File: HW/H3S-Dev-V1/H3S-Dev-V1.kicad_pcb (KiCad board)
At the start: 2 copper layers, 85 x 56 mm, 70 parts, among them J1 USB_C_Receptacle_USB2.0_16P, J2 Conn_01x02, J3 Conn_Coaxial, J4 Conn_01x04, J5 Conn_01x04, Q1 DMP3099L, SW1 SW_Push, SW2 SW_Push, U1 Ra-01SH-P, U2 LTC4054ES5-4.2, U3 USBLC6-2SC6, U4 ESP32-S3-WROOM-1, U5 SY8089AAAC, U6 L96-M33

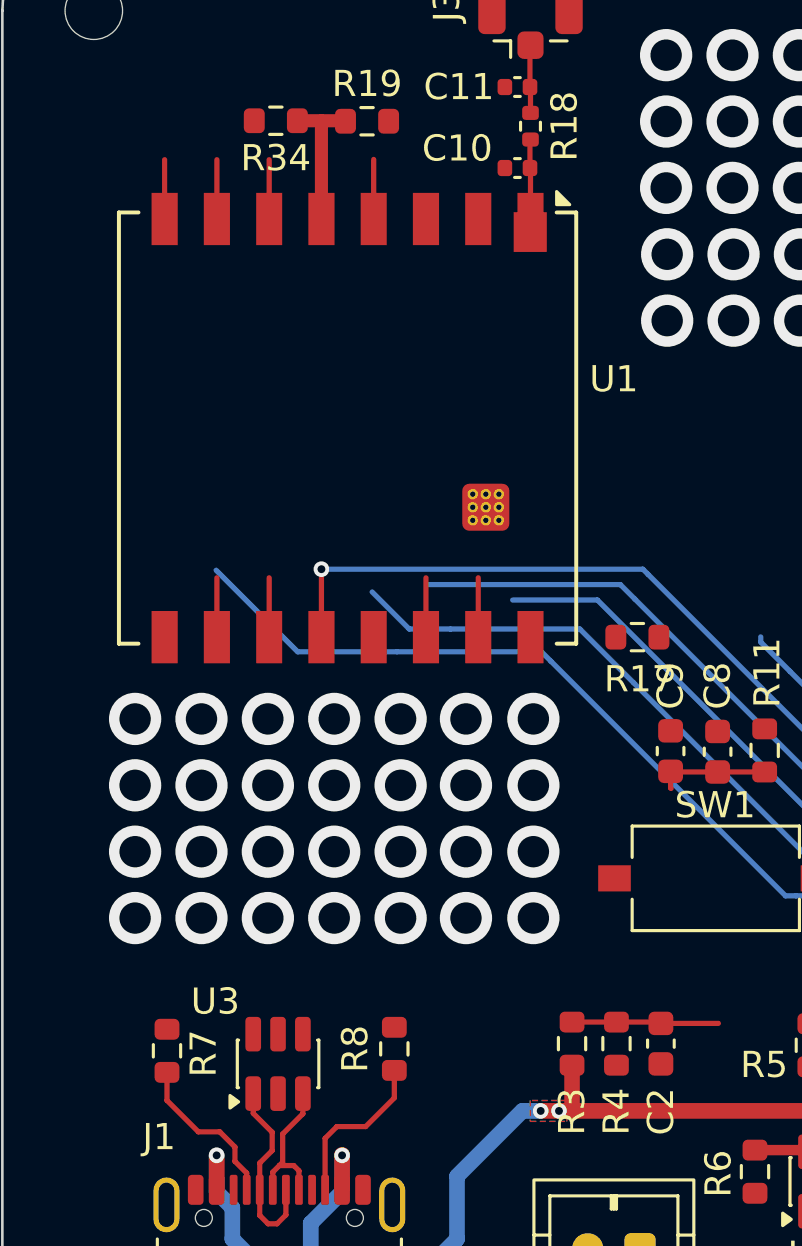
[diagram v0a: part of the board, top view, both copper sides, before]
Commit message: USB Resistors
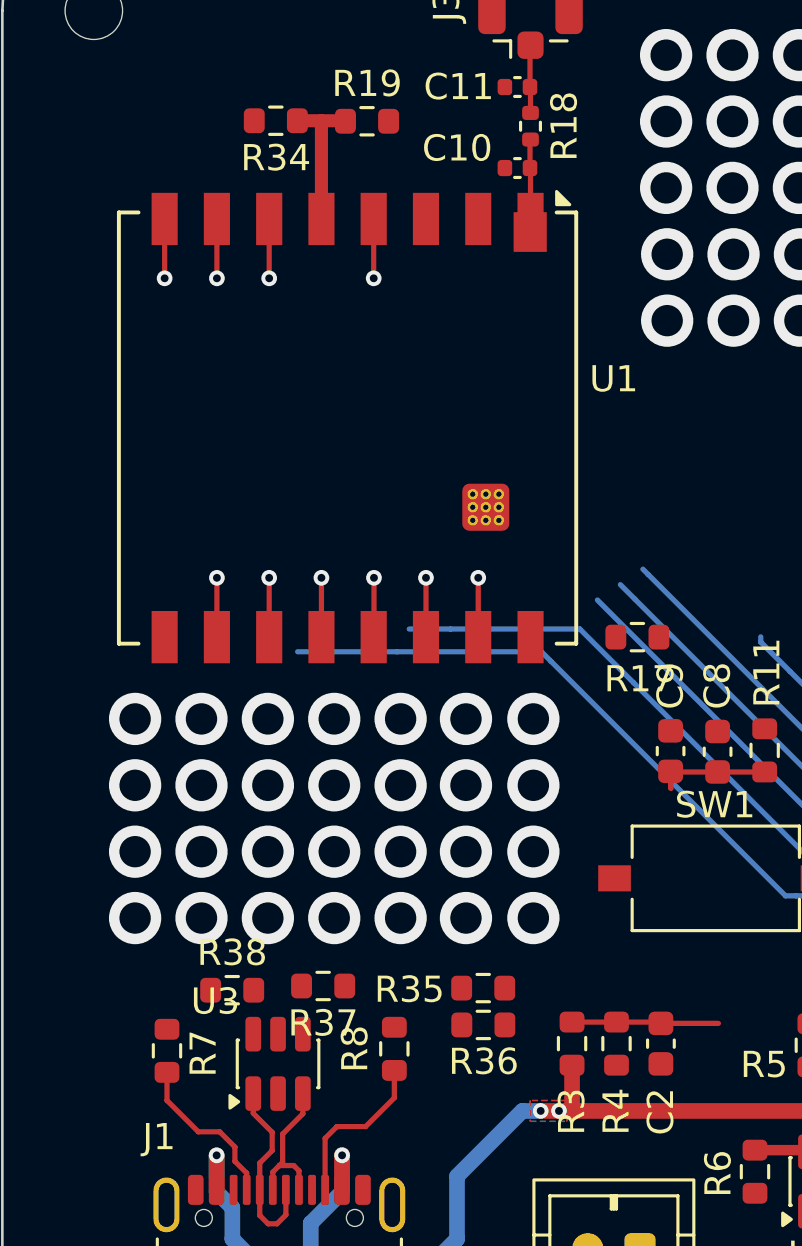
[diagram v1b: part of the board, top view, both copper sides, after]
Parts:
- added R35: 22, Resistor_SMD:R_0603_1608Metric, F.Cu at (118.4, 114.9)
- added R36: 22, Resistor_SMD:R_0603_1608Metric, F.Cu at (118.4, 116.3)
- added R37: 1.5k, Resistor_SMD:R_0603_1608Metric, F.Cu at (112.3, 114.8)
- added R38: 1.5k, Resistor_SMD:R_0603_1608Metric, F.Cu at (108.8, 115.0)
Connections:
- U3 pad 4: Net-(U4-USB_D+) -> Net-(R36-Pad1)
- U3 pad 6: Net-(U4-USB_D-) -> Net-(R35-Pad1)
- U4 pad 36: unconnected-(U4-RXD0-Pad36) -> /TX
- U4 pad 37: unconnected-(U4-TXD0-Pad37) -> /RX
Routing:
- net /SCK: track 35.8 -> 23.5 mm
- net /MOSI: track 33.5 -> 26.1 mm, vias 1 -> 2
- net /L_RF_EN: track 59.3 -> 54.9 mm
- net /~{SS}: track 31.7 -> 28.4 mm, vias 1 -> 2
- net /MISO: track 44.1 -> 44.4 mm, vias 1 -> 2
- net Net-(U1-RF_EN): vias 0 -> 1
- net /~{L_RST}: vias 0 -> 1
- net /L_BUSY: vias 0 -> 1
- net /DIO3: vias 1 -> 2
- net /DIO2: vias 0 -> 1
- net /DIO1: vias 0 -> 1

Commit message: Routing in progress
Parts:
- moved R13 1.15 mm to (161.2, 88.7), turned to 90 degrees
- moved R12 1.15 mm to (163.2, 88.8), turned to 90 degrees
- moved R14 0.98 mm to (178.5, 78.6), turned to -90 degrees
- moved R15 0.41 mm to (175.6, 78.6), turned to -90 degrees
- turned R31 to -90 degrees
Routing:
- net VCC: track 19.1 -> 189.6 mm, vias 3 -> 7
- net /DIO2: track 2.27 -> 45.6 mm
- net /DIO1: track 2.27 -> 42.7 mm
- net /DIO3: track 33.7 -> 71.0 mm
- net /SCL: track 0.00 -> 26.0 mm
- net /SDA: track 0.00 -> 25.1 mm
- net /~{L_RST}: track 2.27 -> 22.0 mm
- net /SCK: track 23.5 -> 37.0 mm
- net /~{ESP_IO0}: track 0.00 -> 9.48 mm
- net /~{ESP_EN}: track 13.6 -> 22.7 mm
- net /L_RF_EN: track 54.9 -> 45.9 mm
- net /MOSI: track 26.1 -> 34.8 mm
- net /MISO: track 44.4 -> 52.2 mm
- net /~{G_RESET}: track 0.00 -> 5.91 mm
- net /~{SS}: track 28.4 -> 34.3 mm
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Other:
- board text added: "BOOT"
- board text added: "RESET"

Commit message: Routing in progress
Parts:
- moved R17 14.4 mm to (110.2, 104.6), turned to -90 degrees
- moved R35 3.34 mm to (116.5, 112.1)
- moved R36 3.27 mm to (116.5, 113.7)
- moved J4 1.30 mm to (164.5, 84.0)
- moved R12 1.30 mm to (164.5, 88.8)
- moved R13 1.30 mm to (162.5, 88.7)
- moved R38 0.17 mm to (108.9, 114.8)
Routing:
- net /L_BUSY: track 2.27 -> 47.4 mm, vias 1 -> 2
- net /~{L_RST}: track 22.0 -> 58.5 mm, vias 1 -> 2
- net Net-(U4-USB_D+): track 0.00 -> 25.1 mm
- net Net-(U4-USB_D-): track 0.00 -> 23.9 mm
- net /DIO1: track 42.7 -> 62.5 mm, vias 1 -> 2
- net /DIO2: track 45.6 -> 64.0 mm, vias 1 -> 2
- net /DIO3: track 71.0 -> 53.6 mm
- net /V5_SENSE: track 22.3 -> 9.69 mm, vias 2 -> 1
- net /L_RF_EN: track 45.9 -> 57.3 mm, vias 1 -> 2
- net Net-(R35-Pad1): track 0.00 -> 9.25 mm
- net /MISO: track 52.2 -> 43.0 mm
- net Net-(R36-Pad1): track 0.00 -> 8.32 mm
- net /SCL: track 26.0 -> 31.6 mm
- net /~{SS}: track 34.3 -> 30.5 mm
- net /MOSI: track 34.8 -> 31.2 mm
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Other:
- board text added: "Meshtastic/Helium OSHW node"
- board text removed: "Meshtastic/Helium node"

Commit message: More progress today
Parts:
- moved R20 7.54 mm to (156.9, 113.0), turned to 0 degrees
- moved R11 7.22 mm to (129.7, 113.0), turned to 180 degrees
- moved C8 5.48 mm to (123.9, 110.1)
- moved C12 4.94 mm to (161.1, 110.1)
- moved C13 4.94 mm to (162.7, 110.1)
- moved C9 4.27 mm to (125.5, 110.1)
- moved SW1 4.04 mm to (128.9, 107.0), turned to 90 degrees
- moved SW2 3.99 mm to (157.7, 107.0), turned to 90 degrees
- moved D4 0.52 mm to (165.6, 106.9)
- moved R22 0.52 mm to (165.6, 110.1)
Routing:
- net /SCL: track 31.6 -> 102.1 mm, vias 0 -> 2
- net /SDA: track 23.8 -> 93.6 mm, vias 0 -> 2
- net /VBUS: track 55.0 -> 99.9 mm, vias 4 -> 5
- net VCC: track 188.4 -> 211.4 mm, vias 7 -> 9
- net /~{ESP_IO0}: track 9.48 -> 29.0 mm
- net /RX: track 0.00 -> 19.4 mm
- net /TX: track 0.00 -> 17.3 mm
- net /~{ESP_EN}: track 22.7 -> 18.6 mm
- net /G_TP: track 5.19 -> 8.99 mm
- net Net-(D4-K): track 0.00 -> 1.62 mm
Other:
- board text added: "PWR"

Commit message: USB Diff pair set up
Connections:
- net Net-(R35-Pad1) renamed /USBp_D-
- net Net-(R36-Pad1) renamed /USBp_D+
- net Net-(U4-USB_D+) renamed /USBc_D+
- net Net-(U4-USB_D-) renamed /USBc_D-
- U4 pad 33: unconnected-(U4-IO40-Pad33) -> /SOLAR_SENSE
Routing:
- net /V5_SENSE: track 9.69 -> 1.86 mm
- net /USBc_D+: track 25.1 -> 20.4 mm
- net /USBc_D-: track 23.9 -> 21.2 mm
- net /USB_D-: track 7.39 -> 5.70 mm
- net /USB_D+: track 5.72 -> 5.08 mm
- net GND: vias 0 -> 14

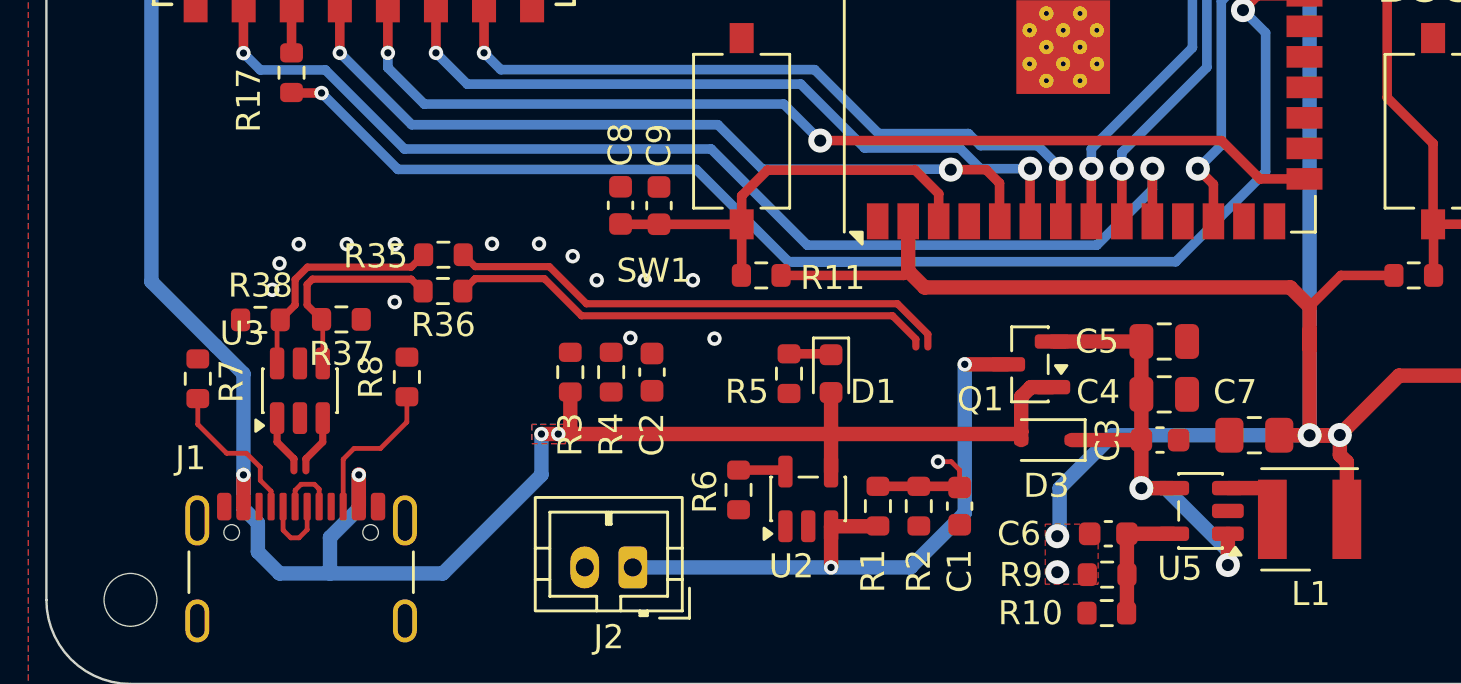
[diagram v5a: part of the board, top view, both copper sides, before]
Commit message: USB Diff pair done
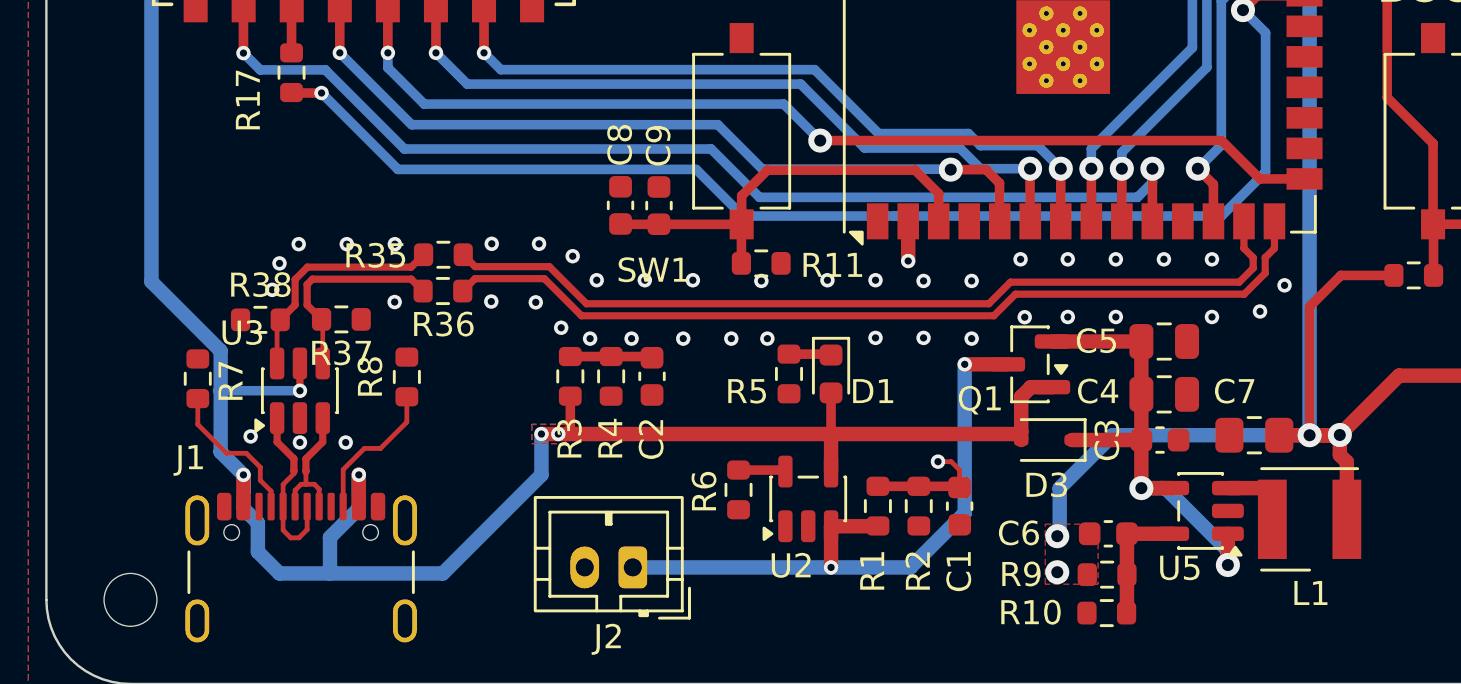
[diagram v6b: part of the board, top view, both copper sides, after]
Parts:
- moved R11 0.50 mm to (129.7, 112.5)
- moved C2 0.17 mm to (125.2, 117.2)
- moved R3 0.17 mm to (121.8, 117.2)
- moved R4 0.17 mm to (123.5, 117.2)
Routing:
- net VCC: track 211.4 -> 187.5 mm, vias 9 -> 10
- net /USBc_D+: track 20.4 -> 37.6 mm
- net /USBc_D-: track 21.2 -> 36.7 mm
- net /VBUS: track 99.9 -> 104.2 mm, vias 5 -> 6
- net /L_RF_EN: track 57.3 -> 53.3 mm
- net /V5_SENSE: track 1.86 -> 5.29 mm
- net /L_BUSY: track 47.4 -> 45.6 mm
- net /USB_D-: track 5.70 -> 7.42 mm
- net /USB_D+: track 5.08 -> 5.69 mm
- net /~{ESP_EN}: track 18.6 -> 18.1 mm
- net GND: vias 14 -> 42

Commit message: Routing progress
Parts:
- added C14: 22u, Capacitor_SMD:C_0805_2012Metric_Pad1.18x1.45mm_HandSolder, F.Cu at (180.2, 112.6)
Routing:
- net VCC: track 187.5 -> 217.0 mm
- net /TX: track 17.3 -> 38.1 mm
- net /RX: track 19.4 -> 37.8 mm
- net /L_RF_EN: track 53.3 -> 52.4 mm
